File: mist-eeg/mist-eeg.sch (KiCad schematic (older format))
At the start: 2 parts

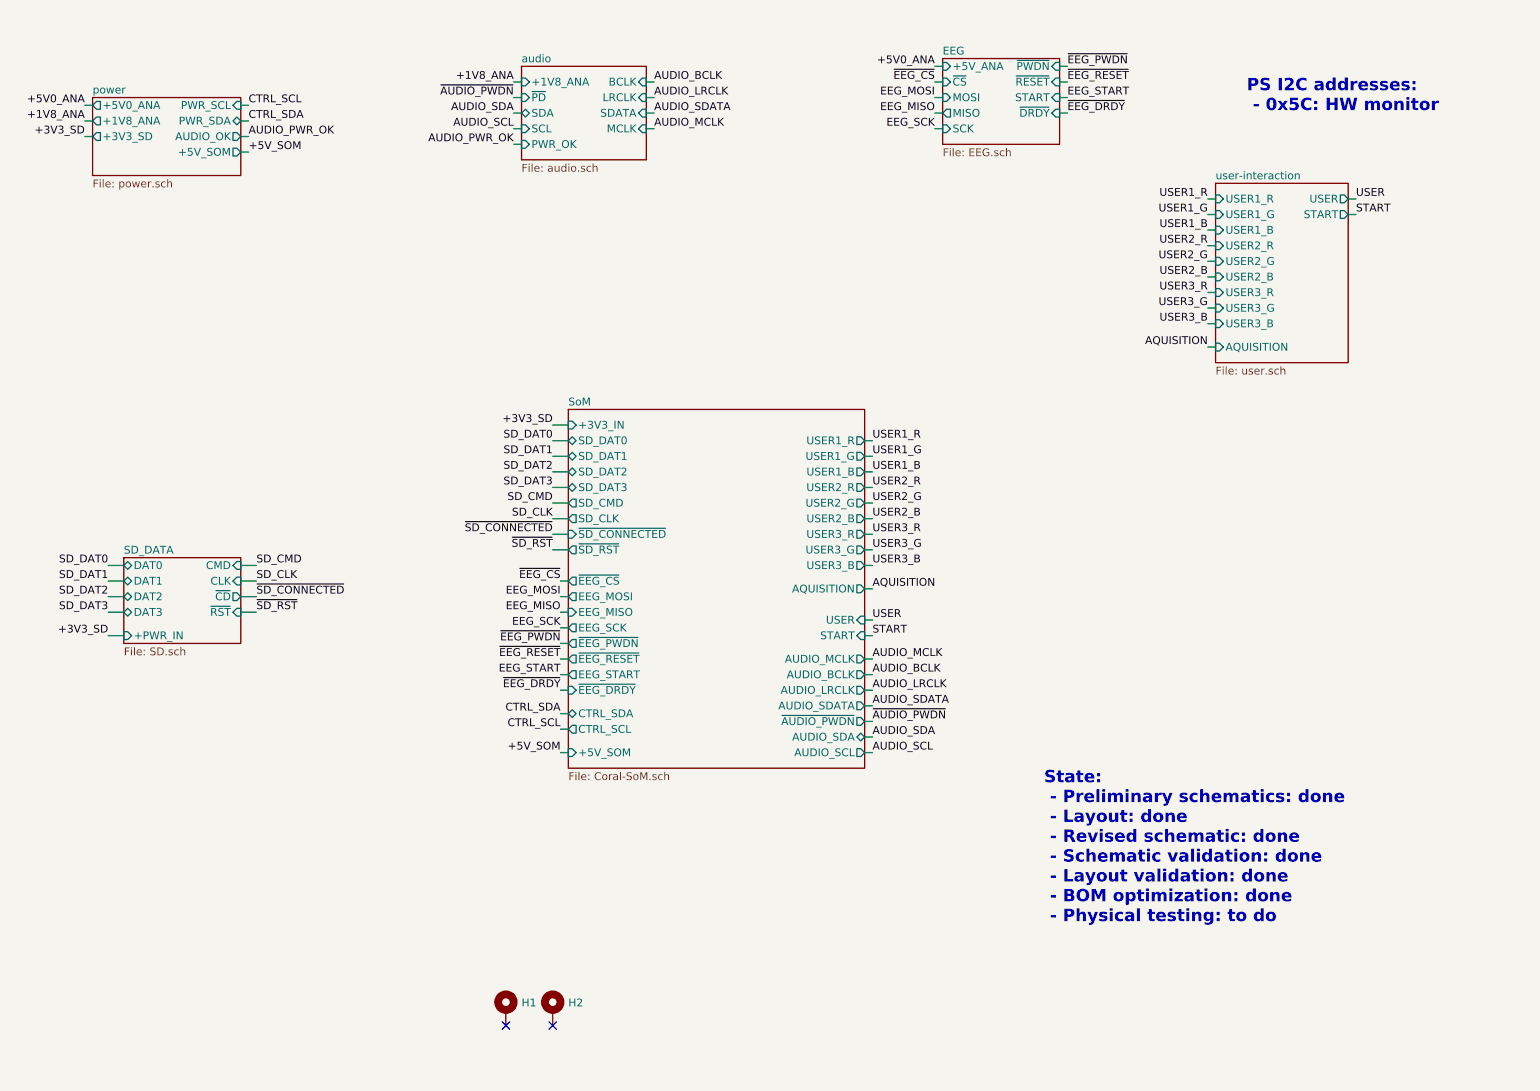
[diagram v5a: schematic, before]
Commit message: Change buckboost regulator used
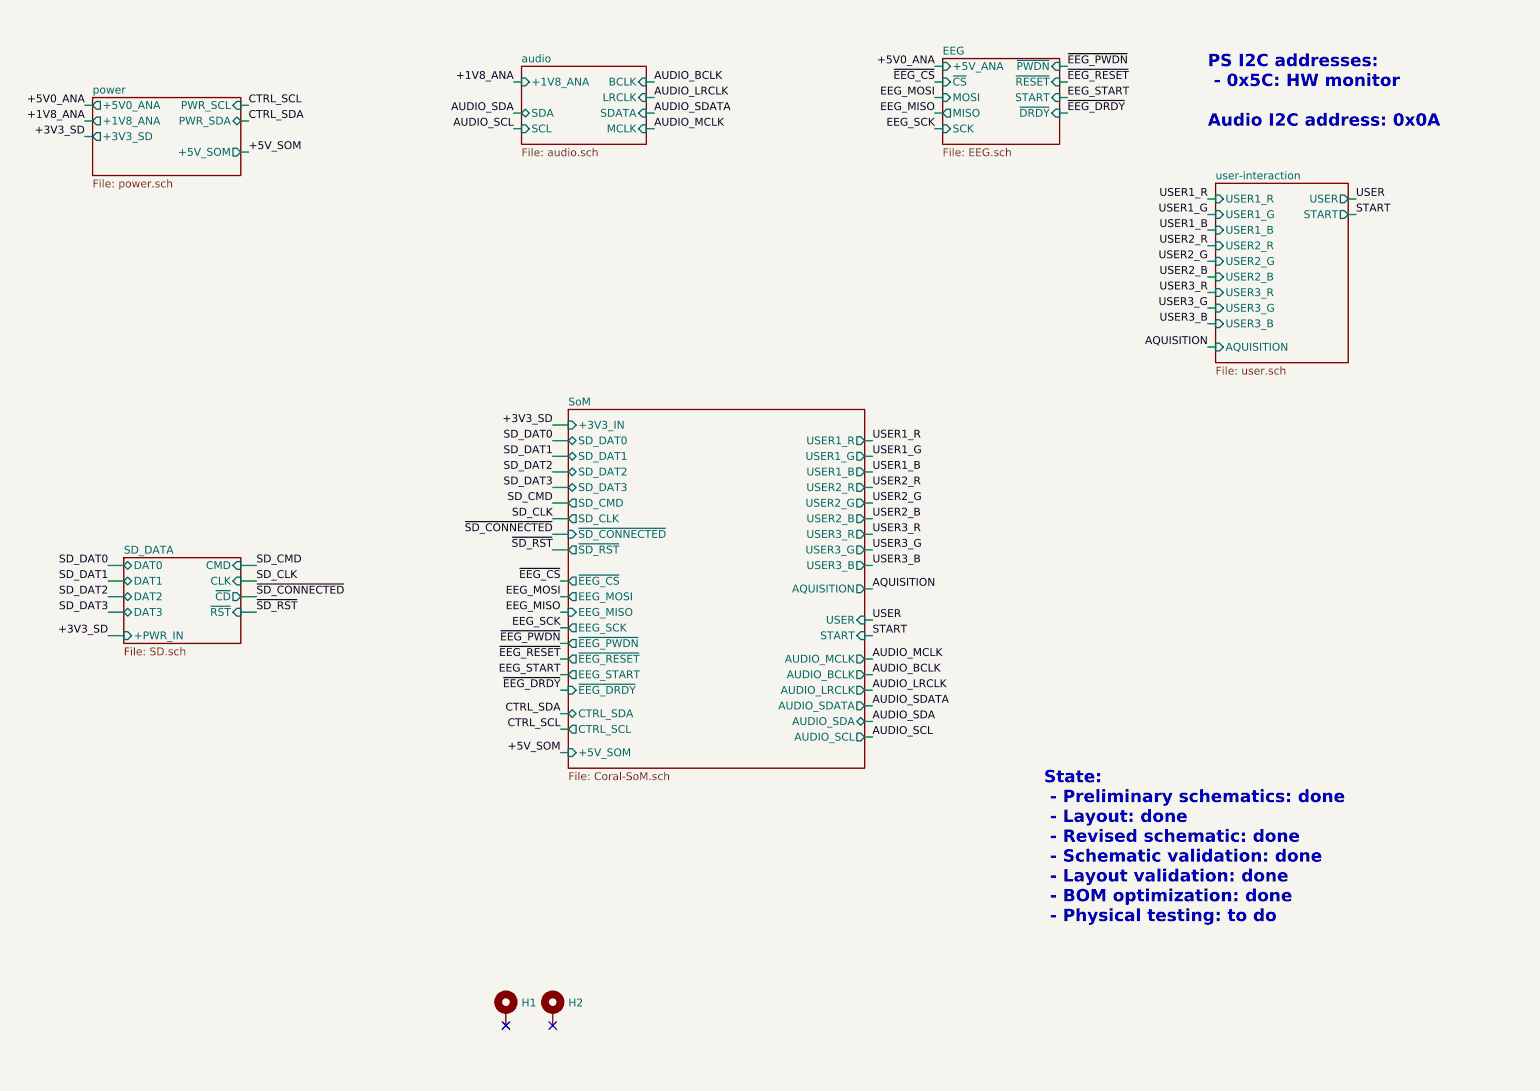
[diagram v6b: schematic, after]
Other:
- note added: "PS I2C addresses:\n - 0x5C: HW monitor\n\nAudio I2C address: 0x0A"
- note removed: "PS I2C addresses:\n - 0x5C: HW monitor"
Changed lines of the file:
@@
 Sheet 1 11
 Title "Portiloop"
-Date "2021-06-07"
-Rev "1A"
+Date "2021-08-03"
+Rev "1D"
 Comp "MIST Lab"
 Comment1 "Designed by Xavier L'Heureux"
@@
 F5 "PWR_SDA" B R 2450 1350 50
 F6 "PWR_SCL" I R 2450 1250 50
-F7 "AUDIO_OK" O R 2450 1450 50
-F8 "+5V_SOM" O R 2450 1550 50
+F7 "+5V_SOM" O R 2450 1550 50
 $EndSheet
 Wire Wire Line
@@
 ~SD_CONNECTED~
 $Sheet
-S 4250 1000 800  600
+S 4250 1000 800  500
 U 60A94F19
 F0 "audio" 50
 F1 "audio.sch" 50
-F2 "~PD~" I L 4250 1200 50
-F3 "+1V8_ANA" I L 4250 1100 50
-F4 "SDA" B L 4250 1300 50
-F5 "SCL" I L 4250 1400 50
-F6 "SDATA" I R 5050 1300 50
-F7 "LRCLK" I R 5050 1200 50
-F8 "BCLK" I R 5050 1100 50
-F9 "PWR_OK" I L 4250 1500 50
-F10 "MCLK" I R 5050 1400 50
+F2 "+1V8_ANA" I L 4250 1100 50
+F3 "SDA" B L 4250 1300 50
+F4 "SCL" I L 4250 1400 50
+F5 "SDATA" I R 5050 1300 50
+F6 "LRCLK" I R 5050 1200 50
+F7 "BCLK" I R 5050 1100 50
+F8 "MCLK" I R 5050 1400 50
 $EndSheet
 $Sheet
@@
 Text Label 4200 1300 2    50   ~ 0
 AUDIO_SDA
-Text Label 4200 1200 2    50   ~ 0
-~AUDIO_PWDN~
-Wire Wire Line
-	4200 1200 4250 1200
 Text Label 5100 1100 0    50   ~ 0
 AUDIO_BCLK
@@
 Wire Wire Line
 	6500 4900 6450 4900
-Text Label 6500 5400 0    50   ~ 0
+Text Label 6500 5300 0    50   ~ 0
 AUDIO_SCL
 Wire Wire Line
-	6500 5400 6450 5400
-Wire Wire Line
 	6500 5300 6450 5300
-Text Label 6500 5300 0    50   ~ 0
+Wire Wire Line
+	6500 5200 6450 5200
+Text Label 6500 5200 0    50   ~ 0
 AUDIO_SDA
-Text Label 6500 5200 0    50   ~ 0
-~AUDIO_PWDN~
-Wire Wire Line
-	6500 5200 6450 5200
 Text Label 1450 1350 2    50   ~ 0
 +1V8_ANA
@@
 Text Notes 7600 6500 0    79   ~ 16
 State:\n - Preliminary schematics: done\n - Layout: done\n - Revised schematic: done\n - Schematic validation: done\n - Layout validation: done\n - BOM optimization: done\n - Physical testing: to do
-Text Notes 8900 1300 0    79   ~ 16
-PS I2C addresses:\n - 0x5C: HW monitor
+Text Notes 8650 1400 0    79   ~ 16
+PS I2C addresses:\n - 0x5C: HW monitor\n\nAudio I2C address: 0x0A
 $Comp
 L Mechanical:MountingHole_Pad H1
@@
 	1    0    0    -1
 $EndComp
-Text Label 2500 1450 0    50   ~ 0
-AUDIO_PWR_OK
-Wire Wire Line
-	2500 1450 2450 1450
 Text Label 1450 1450 2    50   ~ 0
 +3V3_SD
@@
 Wire Wire Line
 	4500 5400 4550 5400
-Text Label 4200 1500 2    50   ~ 0
-AUDIO_PWR_OK
-Wire Wire Line
-	4200 1500 4250 1500
 $Sheet
 S 4550 3200 1900 2300
@@
 F30 "AUDIO_LRCLK" O R 6450 5000 50
 F31 "AUDIO_SDATA" O R 6450 5100 50
-F32 "~AUDIO_PWDN~" O R 6450 5200 50
-F33 "AUDIO_SDA" B R 6450 5300 50
-F34 "AUDIO_SCL" O R 6450 5400 50
-F35 "CTRL_SDA" B L 4550 5150 50
-F36 "CTRL_SCL" O L 4550 5250 50
-F37 "+5V_SOM" I L 4550 5400 50
-F38 "+3V3_IN" I L 4550 3300 50
-F39 "AUDIO_MCLK" O R 6450 4800 50
-F40 "~SD_RST~" O L 4550 4100 50
+F32 "AUDIO_SDA" B R 6450 5200 50
+F33 "AUDIO_SCL" O R 6450 5300 50
+F34 "CTRL_SDA" B L 4550 5150 50
+F35 "CTRL_SCL" O L 4550 5250 50
+F36 "+5V_SOM" I L 4550 5400 50
+F37 "+3V3_IN" I L 4550 3300 50
+F38 "AUDIO_MCLK" O R 6450 4800 50
+F39 "~SD_RST~" O L 4550 4100 50
 $EndSheet
 Text Label 5100 1400 0    50   ~ 0

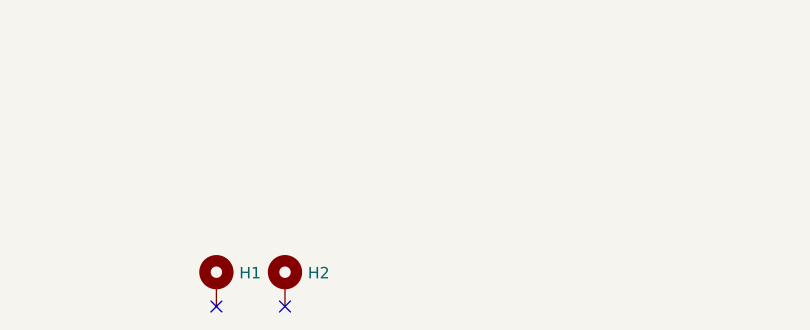
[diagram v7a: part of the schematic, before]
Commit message: Switch to bigger min via size
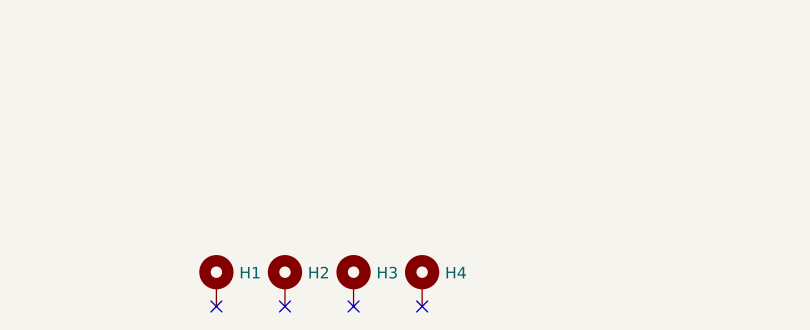
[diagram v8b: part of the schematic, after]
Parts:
- added H3, H4: MountingHole, mist-eeg:MountingHole_1.6mm, symbol Mechanical:MountingHole_Pad
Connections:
- no-connect marks 2 -> 4
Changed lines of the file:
@@
 NoConn ~ 4450 7150
 NoConn ~ 4150 7150
+$Comp
+L Mechanical:MountingHole_Pad H3
+U 1 1 610DB8B8
+P 4750 7050
+F 0 "H3" H 4850 7096 50  0000 L CNN
+F 1 "MountingHole" H 4850 7005 50  0001 L CNN
+F 2 "mist-eeg:MountingHole_1.6mm" H 4750 7050 50  0001 C CNN
+F 3 "~" H 4750 7050 50  0001 C CNN
+	1    4750 7050
+	1    0    0    -1
+$EndComp
+NoConn ~ 4750 7150
+$Comp
+L Mechanical:MountingHole_Pad H4
+U 1 1 610DF3C6
+P 5050 7050
+F 0 "H4" H 5150 7096 50  0000 L CNN
+F 1 "MountingHole" H 5150 7005 50  0001 L CNN
+F 2 "mist-eeg:MountingHole_1.6mm" H 5050 7050 50  0001 C CNN
+F 3 "~" H 5050 7050 50  0001 C CNN
+	1    5050 7050
+	1    0    0    -1
+$EndComp
+NoConn ~ 5050 7150
 $EndSCHEMATC
